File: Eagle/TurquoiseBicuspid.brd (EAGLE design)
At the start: 57.1 x 57.1 mm, 10 parts

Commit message: first attempt at board
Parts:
- removed IC1: (no value), v-reg-micrel:SOT23-5
- added 3.3VREG: 3.3V, v-reg-micrel:SOT23-5
- added R4: 10kΩ, rcl:R1206
- added S1, S2, S3, S4: (no value), switch-omron:B3F-10XX
- moved C1 70.3 mm to (34.3, 14.2), turned to 270 degrees
- moved U$1 67.8 mm to (25.4, 30.5)
- moved HM-10 67.3 mm to (46.0, 33.0)
- moved R1 64.4 mm to (23.6, 36.8), turned to 90 degrees
- moved JP2 61.9 mm to (30.5, 53.3)
- moved USB1 55.7 mm to (27.9, 2.54), turned to 90 degrees
- moved R3 54.1 mm to (30.7, 36.8), turned to 90 degrees
- moved ATTINY85-20SU 52.7 mm to (16.5, 19.1), turned to 180 degrees
- moved R2 44.3 mm to (27.2, 36.8), turned to 90 degrees
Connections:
- new net S$1: ATTINY85-20SU.4, S1.3, S4.3, U$1.C1, U$1.C2, U$1.C3
- net 3.3V: now also 3.3VREG.5; no longer IC1.5
- net 5V: now also 3.3VREG.1, R4.2; no longer IC1.1
- net GND: now also 3.3VREG.2, S2.3, S3.3; no longer ATTINY85-20SU.4, IC1.2, U$1.C1, U$1.C2, U$1.C3
- net N$4: now also R4.1, S1.1, S2.1, S3.1, S4.1
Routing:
- net GND: track 0.00 -> 179.5 mm
- net N$4: track 0.00 -> 160.9 mm
- net N$2: track 0.00 -> 71.1 mm
- net N$1: track 0.00 -> 63.0 mm
- net S$1: track 0.00 -> 62.5 mm
- net 5V: track 0.00 -> 40.1 mm
- net N$11: track 0.00 -> 30.5 mm
- net N$3: track 0.00 -> 28.4 mm
- net N$5: track 0.00 -> 27.0 mm
- net 3.3V: track 0.00 -> 16.3 mm
- net N$7: track 0.00 -> 7.38 mm
- net N$9: track 0.00 -> 7.24 mm
- net N$8: track 0.00 -> 5.03 mm

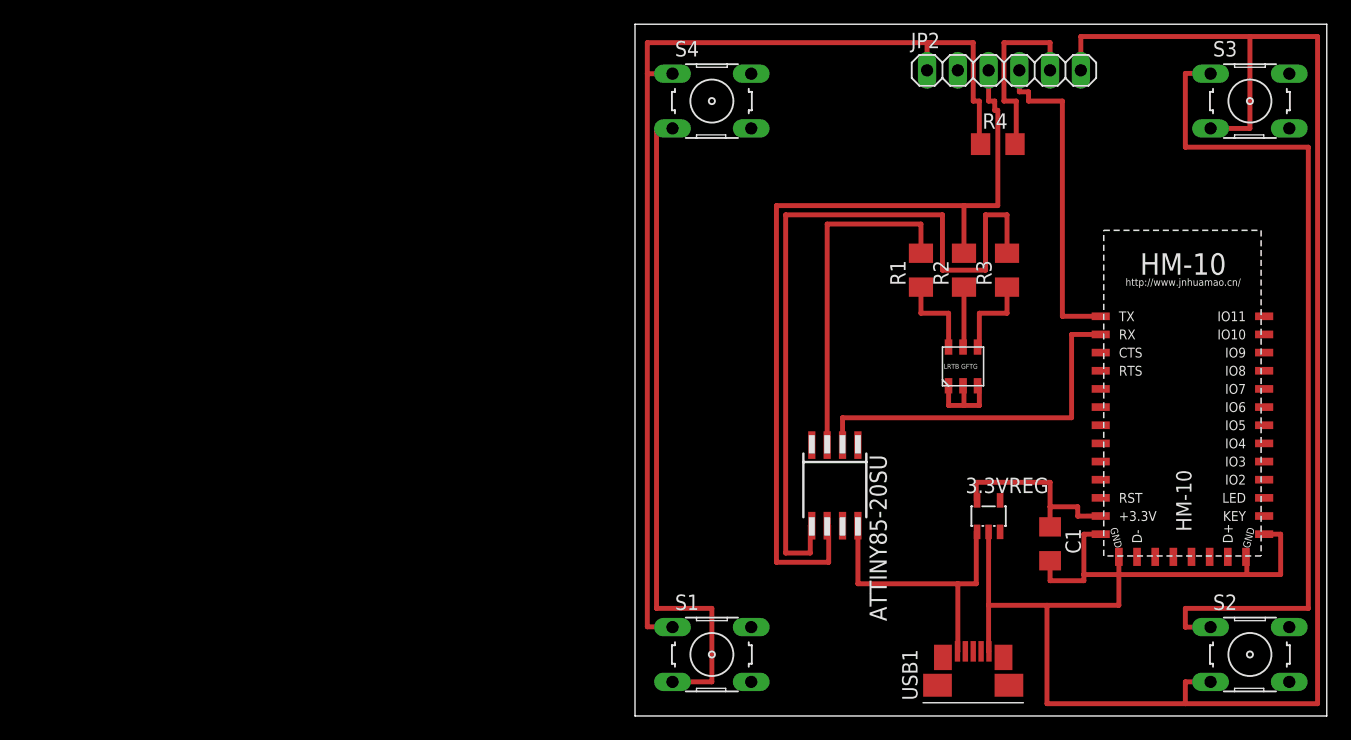
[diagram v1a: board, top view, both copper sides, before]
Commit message: removed 1 switch
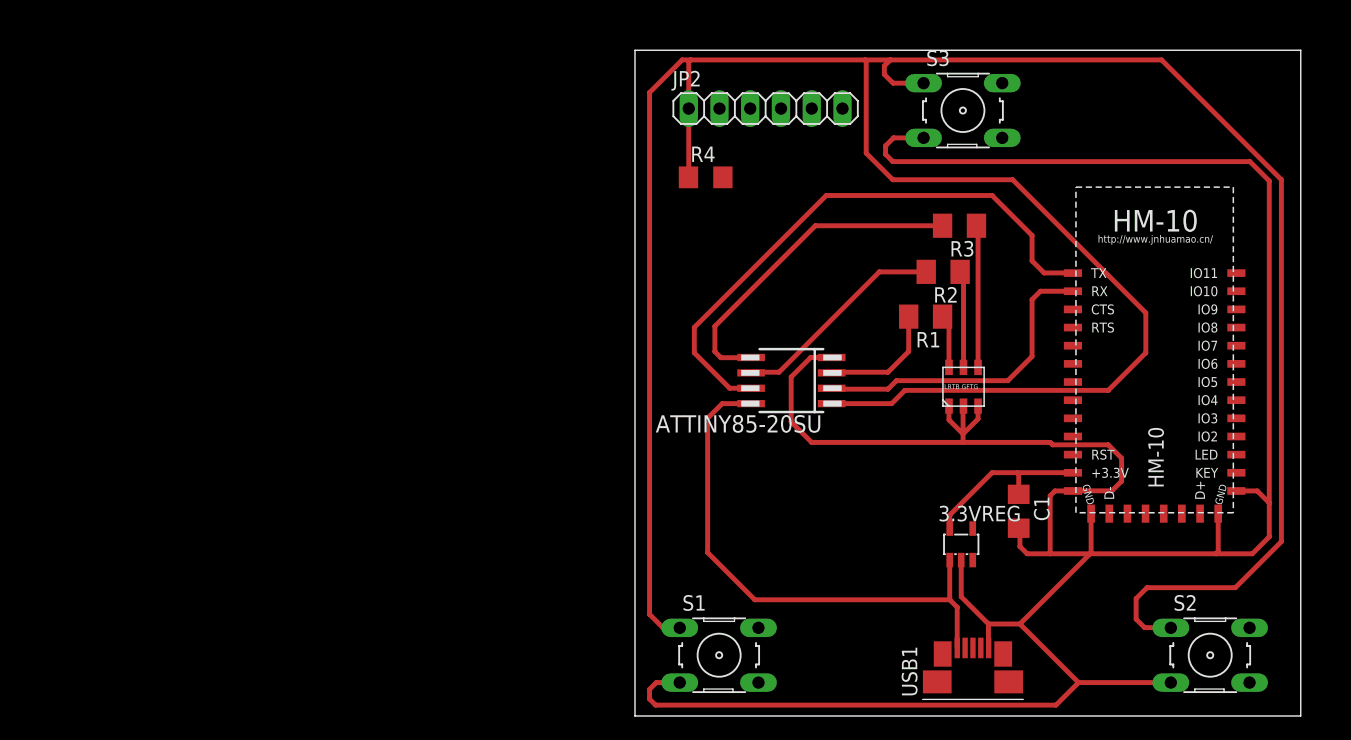
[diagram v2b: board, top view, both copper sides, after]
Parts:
- removed S4: (no value), switch-omron:B3F-10XX
- moved R4 24.3 mm to (5.84, 44.5)
- moved S3 23.7 mm to (27.1, 50.0)
- moved JP2 19.9 mm to (10.8, 50.2)
- moved ATTINY85-20SU 9.37 mm to (12.9, 27.7), turned to 90 degrees
- moved R3 5.37 mm to (26.8, 40.5), turned to 180 degrees
- moved HM-10 4.24 mm to (43.7, 36.6)
- moved R1 3.86 mm to (24.0, 33.0), turned to 180 degrees
- moved C1 3.73 mm to (31.7, 16.9)
- moved S2 3.28 mm to (47.5, 5.02)
- moved 3.3VREG 3.25 mm to (26.9, 14.2)
- moved R2 1.72 mm to (25.5, 36.7), turned to 180 degrees
- moved U$1 1.68 mm to (25.4, 28.8)
- moved S1 0.60 mm to (6.95, 5.02)
- moved USB1 0.28 mm to (27.9, 2.82)
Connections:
- removed net S$1: ATTINY85-20SU.4, S1.3, S4.3, U$1.C1, U$1.C2, U$1.C3
- net GND: now also ATTINY85-20SU.4, S1.3, U$1.C1, U$1.C2, U$1.C3
- net N$4: no longer S4.1
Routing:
- net N$4: track 160.9 -> 234.2 mm
- net S$1: track 62.5 -> 0.00 mm
- net N$2: track 71.1 -> 17.9 mm
- net GND: track 179.5 -> 230.4 mm
- net N$1: track 63.0 -> 27.6 mm
- net N$5: track 27.0 -> 47.7 mm
- net N$3: track 28.4 -> 9.97 mm
- net N$11: track 30.5 -> 26.1 mm
- net N$7: track 7.38 -> 11.8 mm
- net 5V: track 40.1 -> 44.3 mm
- net N$8: track 5.03 -> 8.69 mm
- net N$9: track 7.24 -> 4.41 mm
- net 3.3V: track 16.3 -> 14.6 mm
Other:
- board size 57.1 x 57.1 mm -> 55 x 55 mm

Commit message: fresh board
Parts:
- moved S2 82.9 mm to (-30.5, 33.0)
- moved R2 73.9 mm to (-48.3, 41.9), turned to 0 degrees
- moved USB1 71.1 mm to (-43.2, 5.08), turned to 0 degrees
- moved S3 71.1 mm to (-41.9, 33.0)
- moved C1 69.7 mm to (-29.2, 50.8), turned to 0 degrees
- moved R1 66.5 mm to (-41.9, 41.9), turned to 0 degrees
- moved HM-10 65.7 mm to (-20.3, 21.6)
- moved U$1 64.8 mm to (-35.6, 50.8)
- moved 3.3VREG 54.4 mm to (-19.1, 43.2)
- moved ATTINY85-20SU 52.4 mm to (-34.3, 5.08), turned to 0 degrees
- moved R3 44.5 mm to (-16.5, 50.8), turned to 0 degrees
- moved JP2 40.6 mm to (-29.2, 43.2)
- moved S1 38.2 mm to (-19.1, 33.0)
- moved R4 29.4 mm to (-22.9, 50.8)
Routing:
- net N$4: track 234.2 -> 0.00 mm
- net GND: track 230.4 -> 0.00 mm
- net N$5: track 47.7 -> 0.00 mm
- net 5V: track 44.3 -> 0.00 mm
- net N$1: track 27.6 -> 0.00 mm
- net N$11: track 26.1 -> 0.00 mm
- net N$2: track 17.9 -> 0.00 mm
- net 3.3V: track 14.6 -> 0.00 mm
- net N$7: track 11.8 -> 0.00 mm
- net N$3: track 9.97 -> 0.00 mm
- net N$8: track 8.69 -> 0.00 mm
- net N$9: track 4.41 -> 0.00 mm

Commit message: attempt 3
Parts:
- moved S2 83.8 mm to (48.5, 5.02)
- moved R2 74.9 mm to (26.1, 33.1), turned to 90 degrees
- moved C1 70.3 mm to (31.9, 16.1), turned to 270 degrees
- moved HM-10 70.2 mm to (45.7, 45.6)
- moved ATTINY85-20SU 69.6 mm to (26.1, 39.8), turned to 270 degrees
- moved R1 65.0 mm to (21.4, 27.2), turned to 270 degrees
- moved U$1 63.9 mm to (24.4, 28.8)
- moved S3 56.4 mm to (7.09, 5.02)
- moved R3 53.0 mm to (30.9, 27.2), turned to 270 degrees
- moved 3.3VREG 51.5 mm to (26.4, 18.9), turned to 270 degrees
- moved USB1 51.0 mm to (2.82, 27.1)
- moved S1 49.0 mm to (26.9, 50.0)
- moved JP2 40.0 mm to (9.79, 52.2)
- moved R4 35.8 mm to (9.64, 35.7)
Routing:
- net GND: track 0.00 -> 124.1 mm
- net N$4: track 0.00 -> 53.0 mm
- net 5V: track 0.00 -> 28.0 mm
- net 3.3V: track 0.00 -> 22.1 mm
- net N$5: track 0.00 -> 14.0 mm
- net N$2: track 0.00 -> 13.9 mm
- net N$7: track 0.00 -> 6.75 mm
- net N$9: track 0.00 -> 6.74 mm
- net N$8: track 0.00 -> 2.99 mm

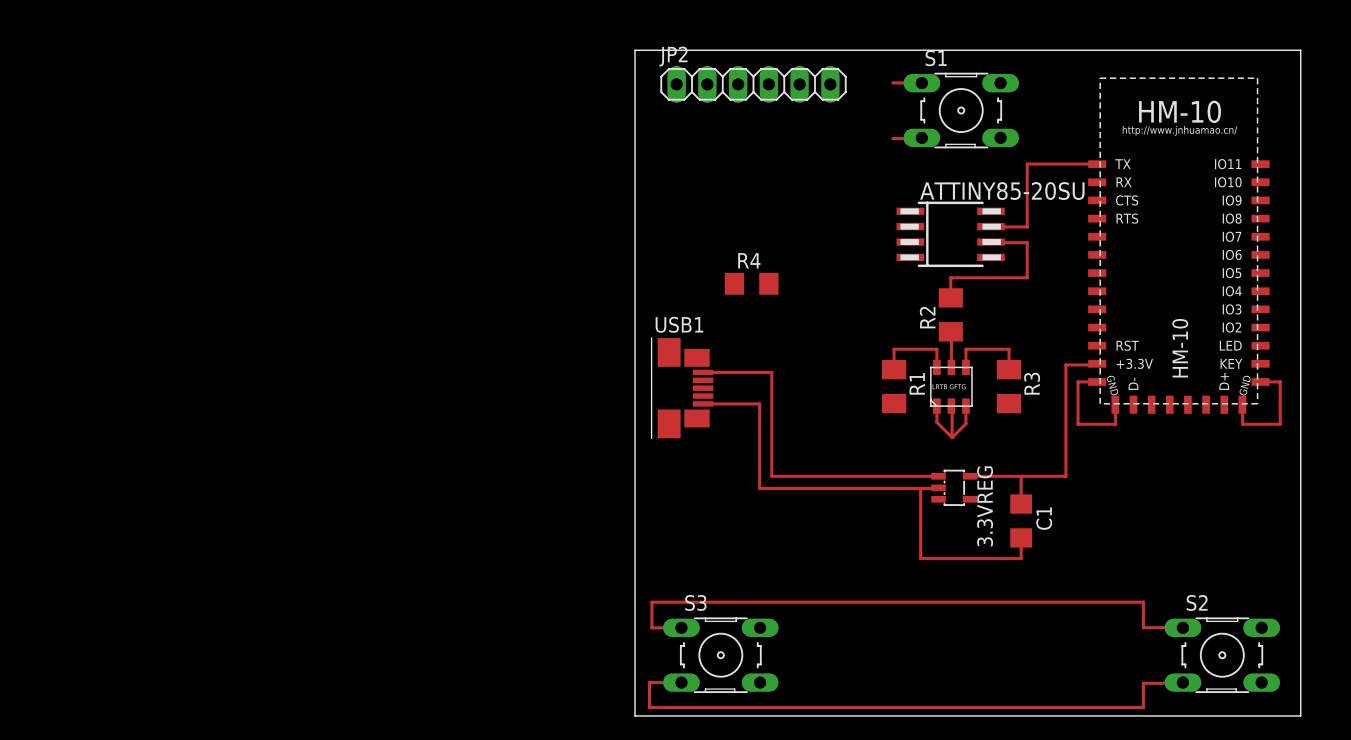
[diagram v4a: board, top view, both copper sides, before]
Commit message: removed programming headers
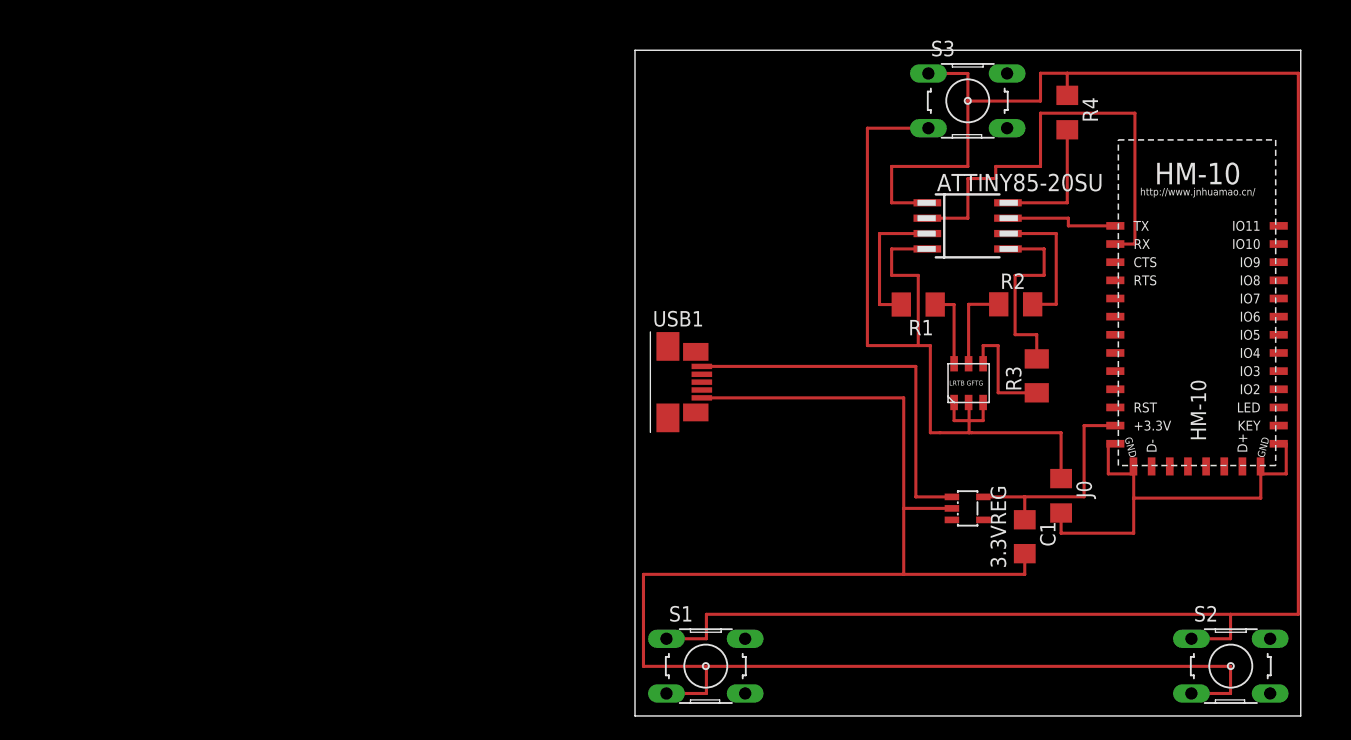
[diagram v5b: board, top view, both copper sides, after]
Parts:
- removed JP2: Programmer, pinhead:1X06
- added J0: 0Ω, rcl:R1206
- moved S1 50.5 mm to (5.85, 4.12)
- moved S3 50.1 mm to (27.5, 50.8)
- moved R4 29.7 mm to (35.7, 49.9), turned to 270 degrees
- moved R1 7.07 mm to (23.4, 34.0), turned to 180 degrees
- moved R2 5.43 mm to (31.4, 34.0), turned to 0 degrees
- moved HM-10 5.32 mm to (47.2, 40.5)
- moved R3 2.46 mm to (33.2, 28.1), turned to 90 degrees
- moved 3.3VREG 2.02 mm to (27.5, 17.1)
- moved ATTINY85-20SU 1.57 mm to (27.5, 40.5)
- moved U$1 1.45 mm to (25.9, 29.1)
- moved C1 1.33 mm to (32.2, 14.8)
- moved S2 1.14 mm to (49.2, 4.12)
- moved USB1 0.51 mm to (2.72, 27.6)
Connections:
- removed net N$5 (its old number): ATTINY85-20SU.7, HM-10.1, JP2.4
- new net N$14: 3.3VREG.1, USB1.1
- new net N$23: ATTINY85-20SU.7, HM-10.1
- new net N$6: HM-10.13, HM-10.14, HM-10.21, HM-10.22, J0.2
- net 5V: no longer 3.3VREG.1, JP2.5, USB1.1
- net GND: now also J0.1; no longer HM-10.13, HM-10.14, HM-10.21, HM-10.22, JP2.6
- net N$1: no longer JP2.2
- net N$2: no longer JP2.3
- net N$4: no longer JP2.1
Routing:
- net N$4: track 53.0 -> 158.8 mm
- net GND: track 124.1 -> 206.6 mm
- net N$5: track 0.00 -> 38.3 mm
- net N$6: track 0.00 -> 36.7 mm
- net N$14: track 0.00 -> 31.4 mm
- net 5V: track 28.0 -> 10.9 mm
- net N$1: track 0.00 -> 16.3 mm
- net N$5 (its old number): track 14.0 -> 0.00 mm
- net N$3: track 0.00 -> 11.6 mm
- net N$23: track 0.00 -> 9.50 mm
- net N$8: track 2.99 -> 7.40 mm
- net 3.3V: track 22.1 -> 18.7 mm
- net N$7: track 6.75 -> 9.83 mm
- net N$2: track 13.9 -> 11.8 mm

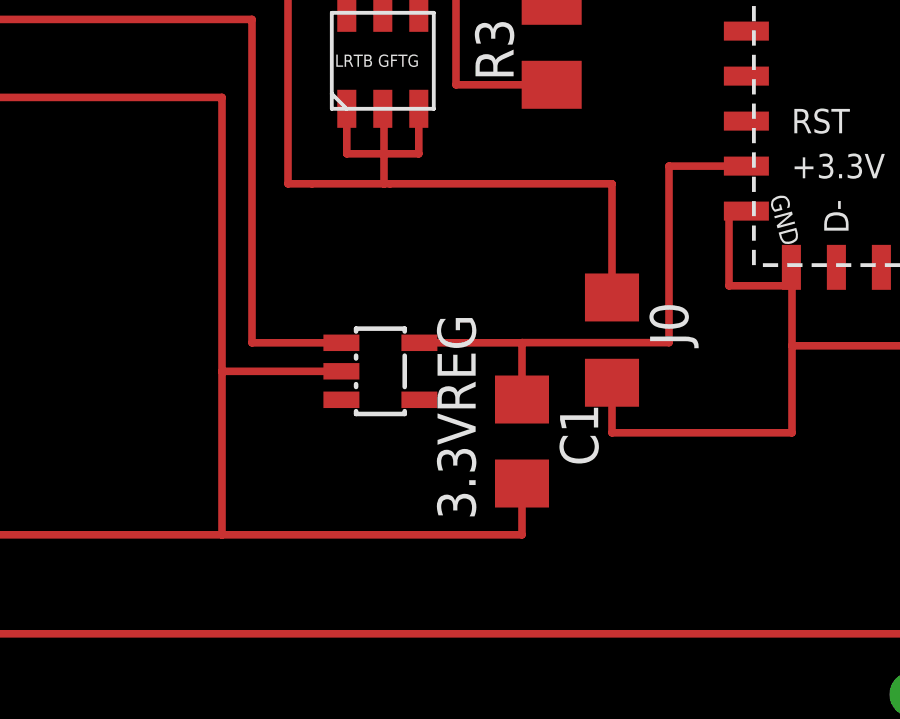
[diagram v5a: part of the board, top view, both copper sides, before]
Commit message: route gnd
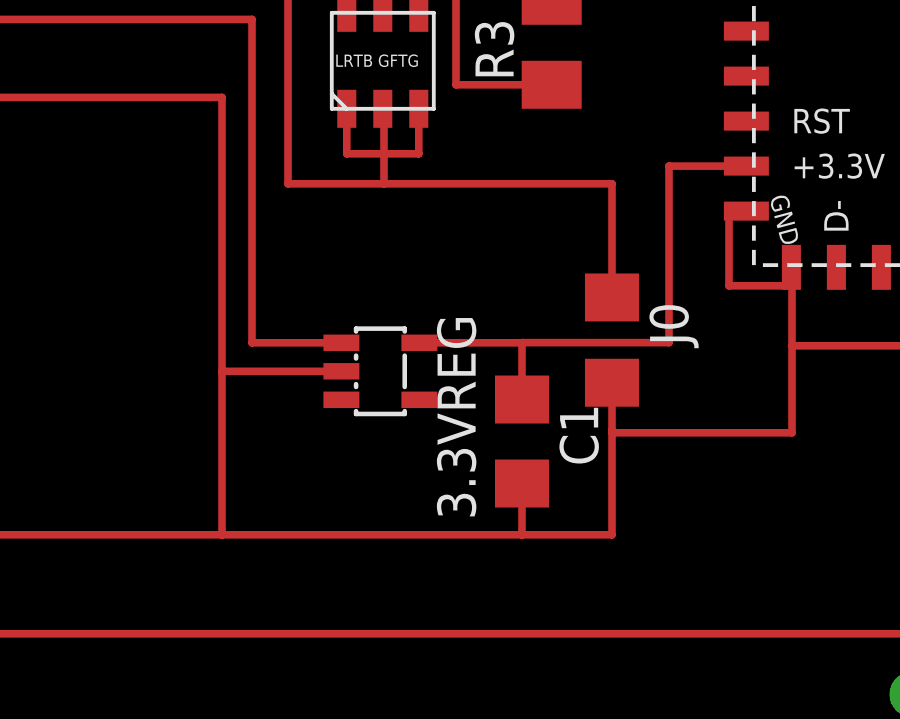
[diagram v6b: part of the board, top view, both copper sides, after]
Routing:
- net GND: track 206.6 -> 213.1 mm
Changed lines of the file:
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@@
 <wire x1="23.4" y1="30.6" x2="24.4" y2="30.6" width="0.254" layer="1"/>
 <wire x1="24.4" y1="30.6" x2="24.4" y2="23.4" width="0.254" layer="1"/>
-<wire x1="25.2" y1="23.4" x2="27.6" y2="23.4" width="0.254" layer="1"/>
+<wire x1="24.4" y1="23.4" x2="27.6" y2="23.4" width="0.254" layer="1"/>
 <wire x1="24.2388" y1="48.5594" x2="19.2" y2="48.5594" width="0.254" layer="1"/>
 <wire x1="19.2" y1="48.5594" x2="19.2" y2="30.6" width="0.254" layer="1"/>
 <wire x1="19.2" y1="30.6" x2="23.4" y2="30.6" width="0.254" layer="1"/>
-<wire x1="32.2" y1="13.41" x2="32.2" y2="11.7" width="0.254" layer="1"/>
 <wire x1="32.2" y1="11.7" x2="22.2" y2="11.7" width="0.254" layer="1"/>
 <wire x1="22.2" y1="11.7" x2="22.2" y2="17.15" width="0.254" layer="1"/>
-<wire x1="27.8" y1="23.4" x2="35.2" y2="23.4" width="0.254" layer="1"/>
-<wire x1="35.2" y1="23.4" x2="35.2" y2="19.612" width="0.254" layer="1"/>
 <wire x1="22.2" y1="11.7" x2="0.7" y2="11.7" width="0.254" layer="1"/>
 <wire x1="0.7" y1="11.7" x2="0.7" y2="4.1" width="0.254" layer="1"/>
 <wire x1="0.7" y1="4.1" x2="5.9" y2="4.1" width="0.254" layer="1"/>
-<wire x1="24.4" y1="23.4" x2="25.2" y2="23.4" width="0.254" layer="1"/>
-<wire x1="27.6" y1="23.4" x2="27.8" y2="23.4" width="0.254" layer="1"/>
 <wire x1="27.6" y1="25.9" x2="28.76" y2="25.9" width="0" layer="19" extent="1-1"/>
-<wire x1="22.2" y1="26.28" x2="24.4" y2="23.4" width="0" layer="19" extent="1-1"/>
+<wire x1="27.6" y1="23.4" x2="35.2" y2="23.4" width="0.254" layer="1"/>
+<wire x1="35.2" y1="23.4" x2="35.2" y2="19.612" width="0.254" layer="1"/>
+<wire x1="32.2" y1="13.41" x2="32.2" y2="11.7" width="0.254" layer="1"/>
+<wire x1="32.2" y1="11.7" x2="35.2" y2="11.7" width="0.254" layer="1"/>
+<wire x1="35.2" y1="11.7" x2="35.2" y2="15.2" width="0.254" layer="1"/>
+<wire x1="35.2" y1="15.2" x2="35.2" y2="19.612" width="0" layer="19" extent="1-16"/>
 </signal>
 <signal name="N$1">
